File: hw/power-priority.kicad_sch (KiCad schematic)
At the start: 20 parts, among them IC7703 LM74800QDRRRQ1, IC7704 LM74800QDRRRQ1, Q7714 IPB026N06NATMA1, Q7715 IPB026N06NATMA1, Q7716 IPB026N06NATMA1, Q7717 IPB026N06NATMA1

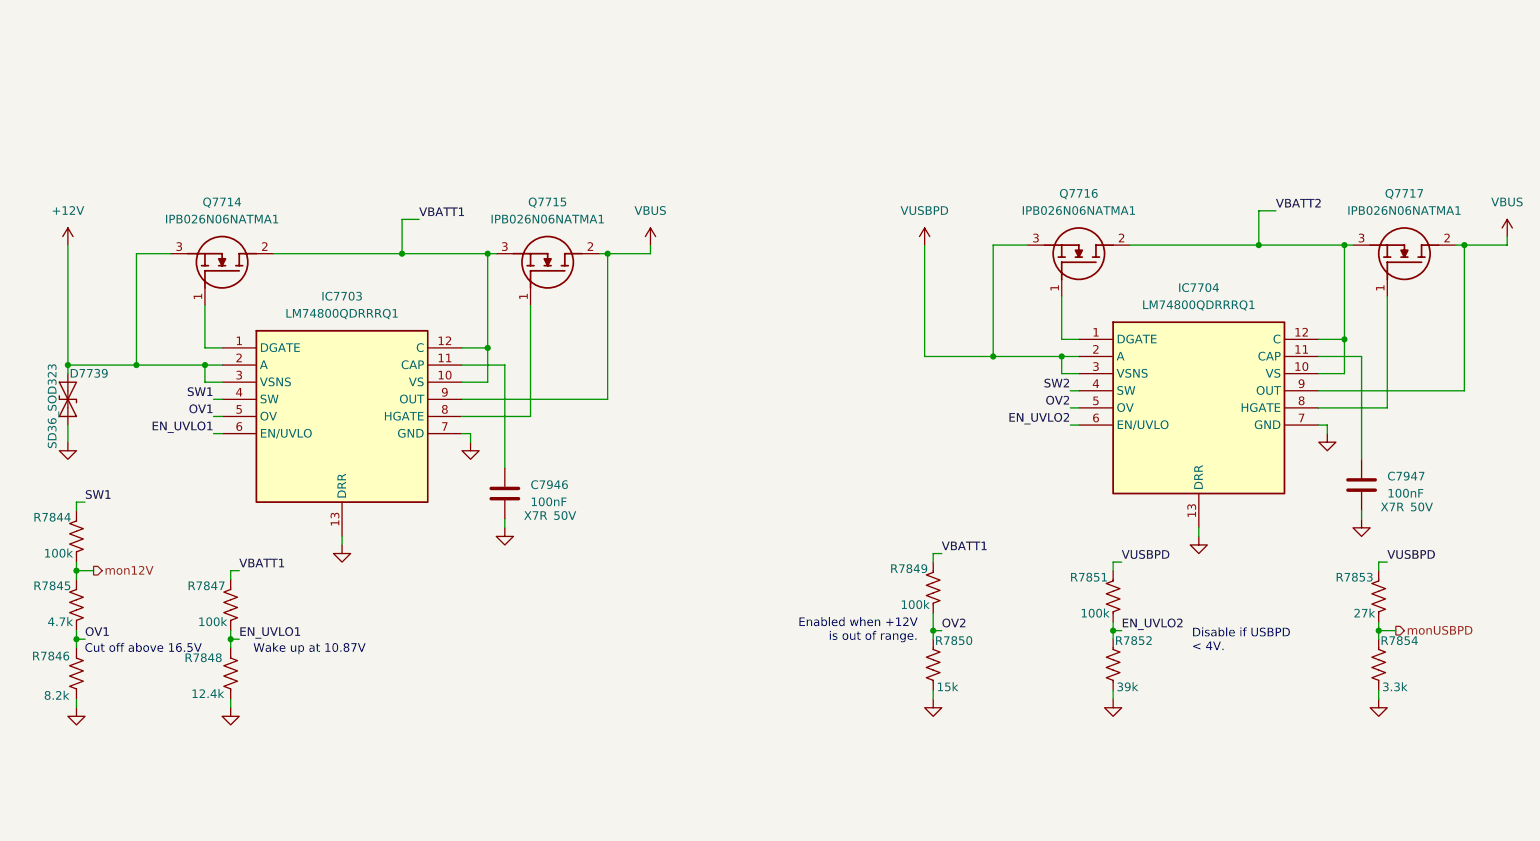
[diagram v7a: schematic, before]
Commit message: OK I have part numbers for consolidated caps, resistors, inductors and all ICs are now Uxxx refdes.
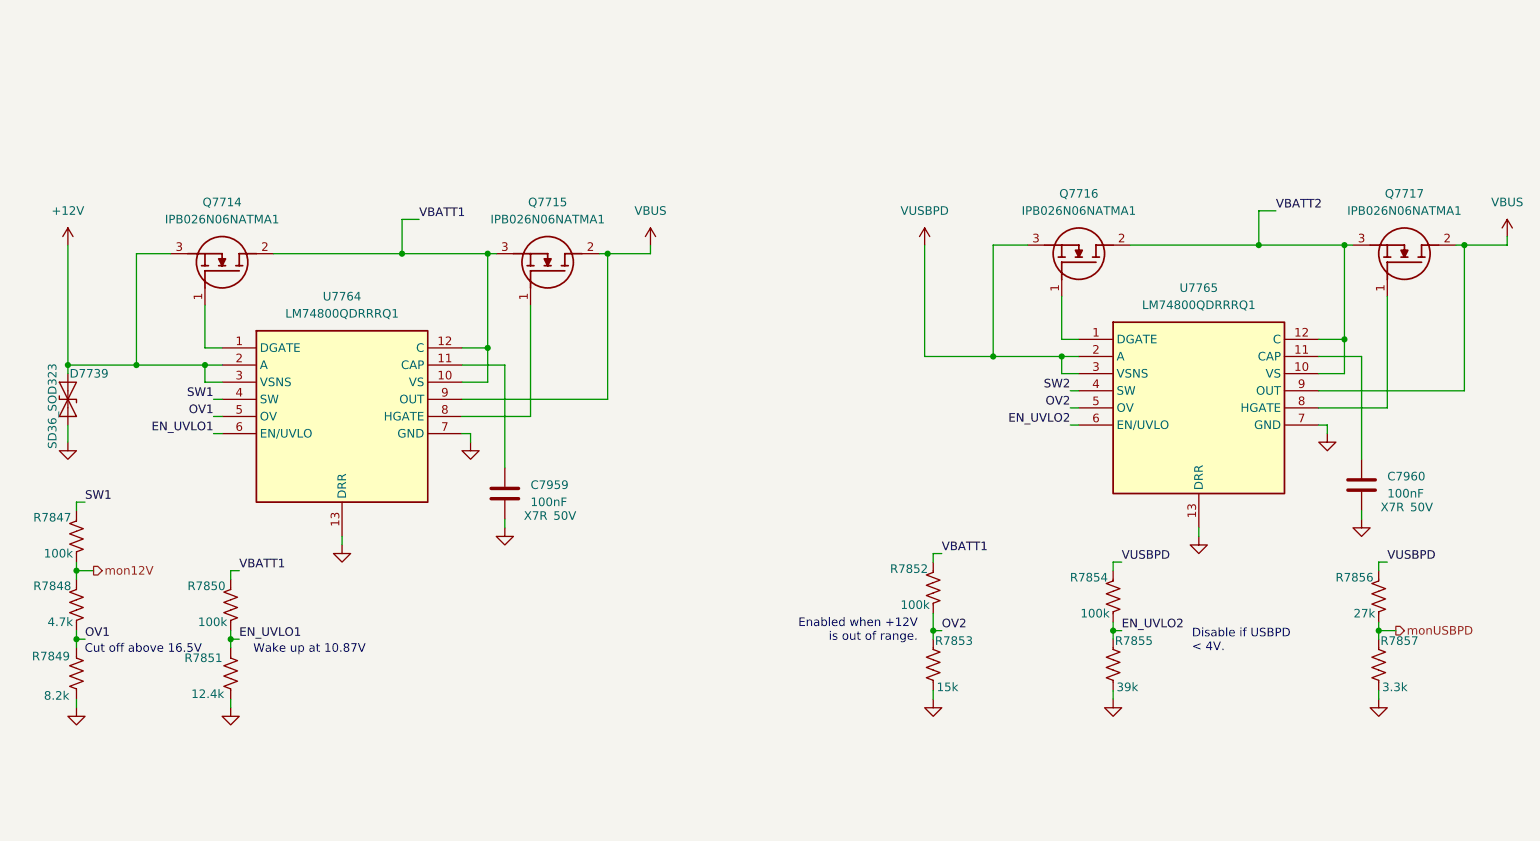
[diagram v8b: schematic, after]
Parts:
- C7959: renamed from C7946; Manufacturer_Name (none) -> Kemet; Manufacturer_Part_Number (none) -> C0805F104K1RACAUTO; Mouser Part Number (none) -> 80-C0805F104K1RAUTO
- C7960: renamed from C7947; Manufacturer_Name (none) -> Kemet; Manufacturer_Part_Number (none) -> C0805F104K1RACAUTO; Mouser Part Number (none) -> 80-C0805F104K1RAUTO
- renumbered R7844 to R7847, R7845 to R7848, R7846 to R7849, R7847 to R7850, R7848 to R7851, R7849 to R7852, R7850 to R7853, R7851 to R7854, R7852 to R7855, R7853 to R7856, R7854 to R7857, IC7703 to U7764, IC7704 to U7765
